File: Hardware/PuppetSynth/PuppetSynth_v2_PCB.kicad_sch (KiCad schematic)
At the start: 59 parts, among them J10 PINHD_1x6_Female, J11 JST_03, J12 JST_03, J13 JST_05, J14 JST_05, J15 JST_05, J16 JST_03, J17 JST_03, J18 JST_03, J19 PINHD_1x6_Female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

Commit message: updated pcb
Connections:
- net Main_1: now also J19.2; no longer J19.3
- net Main_2: now also J19.3; no longer J19.4
- net Switch_1: now also J19.5; no longer J19.6
- net Switch_3: now also J19.4; no longer J19.5
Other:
- moved on the sheet: J11, J12, J13, J14, J15

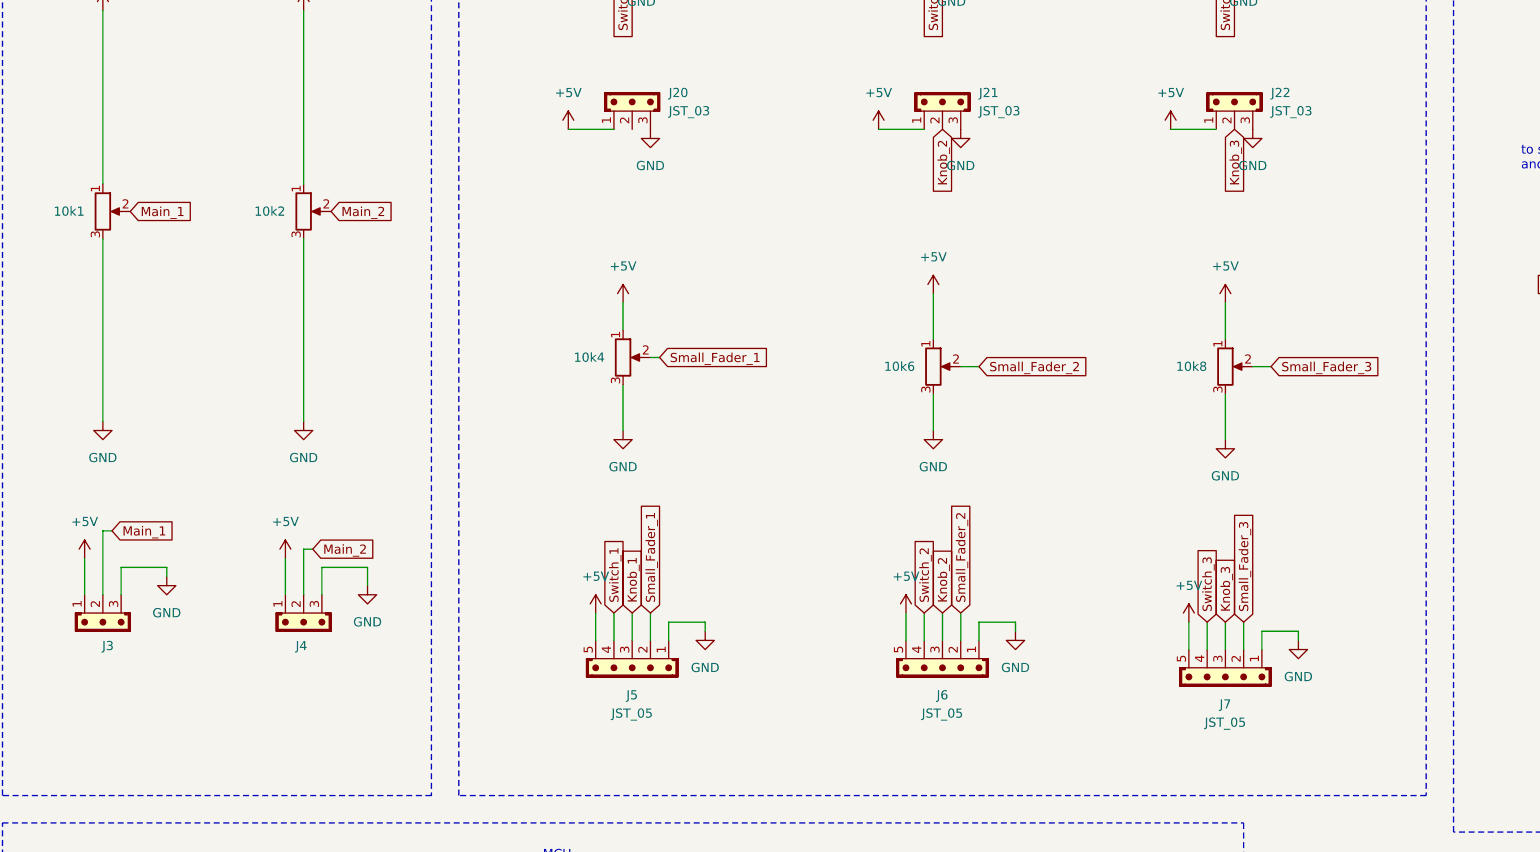
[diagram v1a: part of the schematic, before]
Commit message: Updated schematic and PCB
fixed symbols in schematic, rearranged some parts on PCB, ran traces, aesthetic improvements, fixed layers
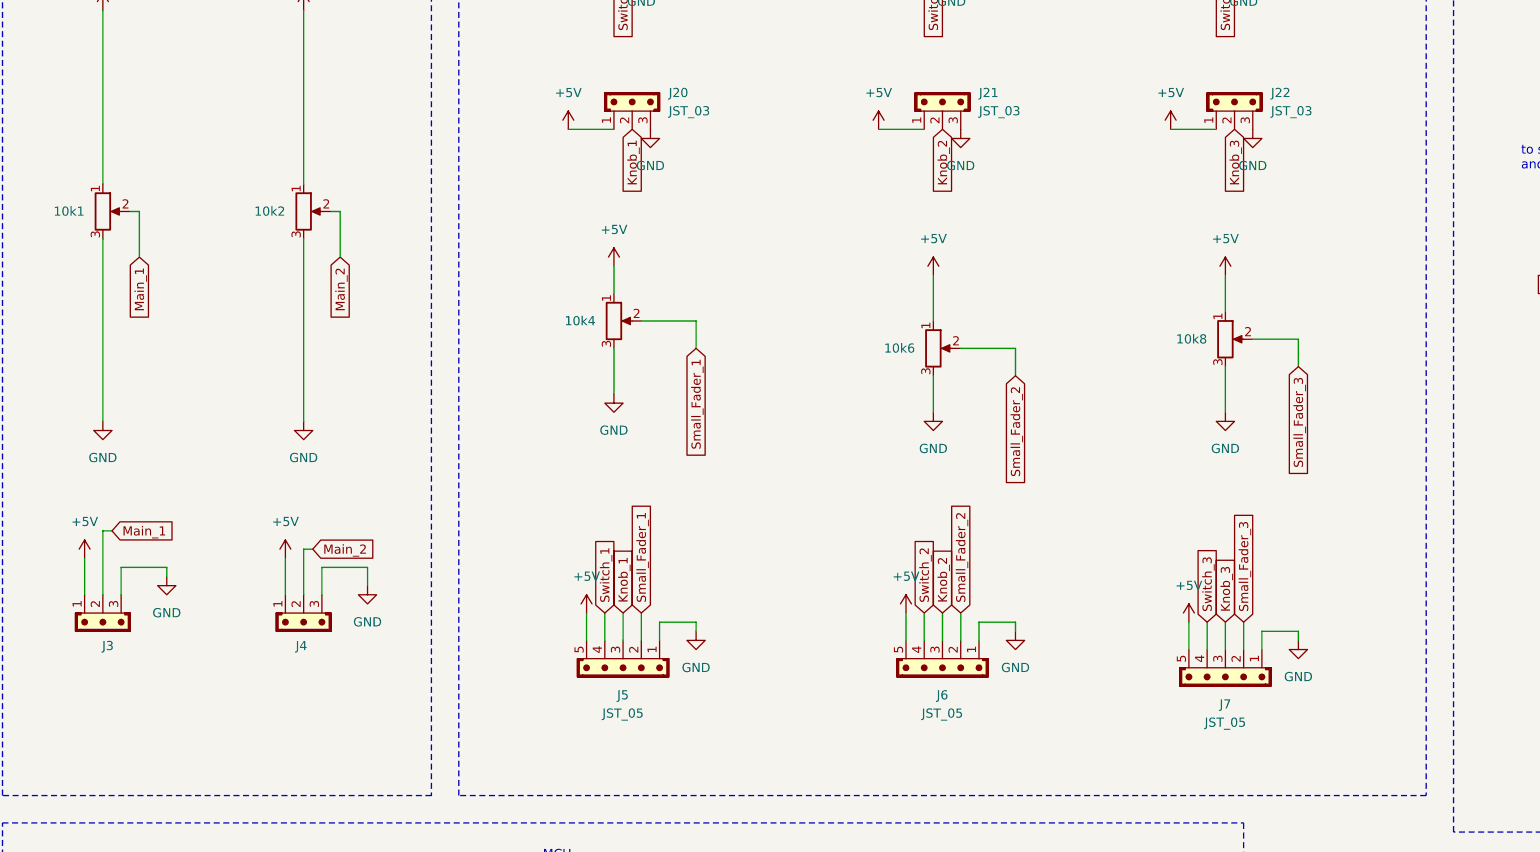
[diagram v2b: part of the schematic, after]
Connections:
- net Knob_1: now also J20.2
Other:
- moved on the sheet: 10k4, 10k6, 10k8, J5
